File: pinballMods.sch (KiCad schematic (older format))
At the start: 17 parts, among them J1 Conn_01x07_MountingPin, J2 Conn_02x07_Counter_Clockwise_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, J3 Conn_01x07_MountingPin

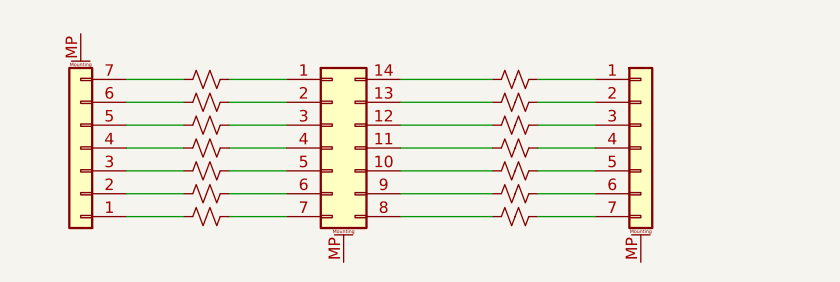
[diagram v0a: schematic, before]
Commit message: Update To Socket and pins
Added DIP16 socket and extra set of pins and pads for 0805 0Ohm resistors.
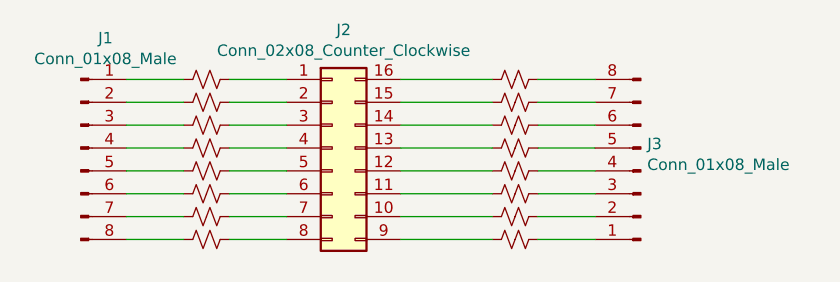
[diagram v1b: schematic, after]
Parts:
- removed J1, J3: Conn_01x07_MountingPin, Connector_PinHeader_2.54mm:PinHeader_1x07_P2.54mm_Vertical, symbol Connector_Generic_MountingPin:Conn_01x07_MountingPin
- removed J2: Conn_02x07_Counter_Clockwise_MountingPin, Package_DIP:DIP-14_W7.62mm_Socket_LongPads, symbol Connector_Generic_MountingPin:Conn_02x07_Counter_Clockwise_MountingPin
- added J1, J3: Conn_01x08_Male, Connector_PinHeader_2.54mm:PinHeader_1x08_P2.54mm_Vertical, symbol Connector:Conn_01x08_Male
- added J2: Conn_02x08_Counter_Clockwise, Package_DIP:DIP-16_W7.62mm_Socket, symbol Connector_Generic:Conn_02x08_Counter_Clockwise
- added R16, R8: R_Small_US, Resistor_SMD:R_0805_2012Metric_Pad1.20x1.40mm_HandSolder, symbol Device:R_Small_US
- R2: value R1 -> R2
- renumbered R9 to R10, R10 to R11, R11 to R12, R12 to R13, R13 to R14, R14 to R15, R8 to R9
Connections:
- net at R1.2: now also J2.1 (Pin_1)
- net at R13.1: now also J2.12 (Pin_12)
- net at R12.1: now also J2.13 (Pin_13)
- net at R11.1: now also J2.14 (Pin_14)
- net at R10.1: now also J2.15 (Pin_15)
- net at R9.1: now also J2.16 (Pin_16)
- net at R2.2: now also J2.2 (Pin_2)
- net at R3.2: now also J2.3 (Pin_3)
- net at R4.2: now also J2.4 (Pin_4)
- net at R5.2: now also J2.5 (Pin_5)
- net at R6.2: now also J2.6 (Pin_6)
- net at R7.2: now also J2.7 (Pin_7)
- net at R15.1: now also J2.10 (Pin_10)
- net at R14.1: now also J2.11 (Pin_11)
- net at R9.2: now also J3.8 (Pin_8)
- net at R10.2: now also J3.7 (Pin_7)
- net at R11.2: now also J3.6 (Pin_6)
- net at R12.2: now also J3.5 (Pin_5)
- net at R13.2: now also J3.4 (Pin_4)
- net at R14.2: now also J3.3 (Pin_3)
- net at R15.2: now also J3.2 (Pin_2)
- net at R1.1: now also J1.1 (Pin_1)
- net at R2.1: now also J1.2 (Pin_2)
- net at R3.1: now also J1.3 (Pin_3)
- net at R4.1: now also J1.4 (Pin_4)
- net at R5.1: now also J1.5 (Pin_5)
- net at R6.1: now also J1.6 (Pin_6)
- net at R7.1: now also J1.7 (Pin_7)
- new net: J1.8 (Pin_8), R8.1
- new net: J2.8 (Pin_8), R8.2
- new net: J2.9 (Pin_9), R16.1
- new net: J3.1 (Pin_1), R16.2
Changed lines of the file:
@@
 $EndDescr
 $Comp
-L Connector_Generic_MountingPin:Conn_02x07_Counter_Clockwise_MountingPin J2
-U 1 1 5FF3D6BF
-P 5350 3650
-F 0 "J2" H 5400 4167 50  0001 C CNN
-F 1 "Conn_02x07_Counter_Clockwise_MountingPin" H 5350 2950 50  0001 C CNN
-F 2 "Package_DIP:DIP-14_W7.62mm_Socket_LongPads" H 5350 3650 50  0001 C CNN
-F 3 "~" H 5350 3650 50  0001 C CNN
-	1    5350 3650
-	1    0    0    -1
-$EndComp
-$Comp
-L Device:R_Small_US R8
+L Device:R_Small_US R9
 U 1 1 5FF4481B
 P 6150 3350
-F 0 "R8" V 6263 3350 50  0001 C CNN
+F 0 "R9" V 6263 3350 50  0001 C CNN
 F 1 "R_Small_US" V 6264 3350 50  0001 C CNN
 F 2 "Resistor_SMD:R_0805_2012Metric_Pad1.20x1.40mm_HandSolder" H 6150 3350 50  0001 C CNN
@@
 $EndComp
 $Comp
-L Device:R_Small_US R9
+L Device:R_Small_US R10
 U 1 1 5FF45935
 P 6150 3450
-F 0 "R9" V 6263 3450 50  0001 C CNN
+F 0 "R10" V 6263 3450 50  0001 C CNN
 F 1 "R_Small_US" V 6264 3450 50  0001 C CNN
 F 2 "Resistor_SMD:R_0805_2012Metric_Pad1.20x1.40mm_HandSolder" H 6150 3450 50  0001 C CNN
@@
 $EndComp
 $Comp
-L Device:R_Small_US R10
+L Device:R_Small_US R11
 U 1 1 5FF461A4
 P 6150 3550
-F 0 "R10" V 6263 3550 50  0001 C CNN
+F 0 "R11" V 6263 3550 50  0001 C CNN
 F 1 "R_Small_US" V 6264 3550 50  0001 C CNN
 F 2 "Resistor_SMD:R_0805_2012Metric_Pad1.20x1.40mm_HandSolder" H 6150 3550 50  0001 C CNN
@@
 $EndComp
 $Comp
-L Device:R_Small_US R11
+L Device:R_Small_US R12
 U 1 1 5FF466FC
 P 6150 3650
-F 0 "R11" V 6263 3650 50  0001 C CNN
+F 0 "R12" V 6263 3650 50  0001 C CNN
 F 1 "R_Small_US" V 6264 3650 50  0001 C CNN
 F 2 "Resistor_SMD:R_0805_2012Metric_Pad1.20x1.40mm_HandSolder" H 6150 3650 50  0001 C CNN
@@
 $EndComp
 $Comp
-L Device:R_Small_US R12
+L Device:R_Small_US R13
 U 1 1 5FF4686E
 P 6150 3750
-F 0 "R12" V 6263 3750 50  0001 C CNN
+F 0 "R13" V 6263 3750 50  0001 C CNN
 F 1 "R_Small_US" V 6264 3750 50  0001 C CNN
 F 2 "Resistor_SMD:R_0805_2012Metric_Pad1.20x1.40mm_HandSolder" H 6150 3750 50  0001 C CNN
@@
 $EndComp
 $Comp
-L Device:R_Small_US R13
+L Device:R_Small_US R14
 U 1 1 5FF46986
 P 6150 3850
-F 0 "R13" V 6263 3850 50  0001 C CNN
+F 0 "R14" V 6263 3850 50  0001 C CNN
 F 1 "R_Small_US" V 6264 3850 50  0001 C CNN
 F 2 "Resistor_SMD:R_0805_2012Metric_Pad1.20x1.40mm_HandSolder" H 6150 3850 50  0001 C CNN
@@
 $EndComp
 $Comp
-L Device:R_Small_US R14
+L Device:R_Small_US R15
 U 1 1 5FF46B0A
 P 6150 3950
-F 0 "R14" V 6263 3950 50  0001 C CNN
+F 0 "R15" V 6263 3950 50  0001 C CNN
 F 1 "R_Small_US" V 6264 3950 50  0001 C CNN
 F 2 "Resistor_SMD:R_0805_2012Metric_Pad1.20x1.40mm_HandSolder" H 6150 3950 50  0001 C CNN
@@
 P 4800 3450
 F 0 "R2" V 4913 3450 50  0001 C CNN
-F 1 "R1" V 4914 3450 50  0001 C CNN
+F 1 "R2" V 4914 3450 50  0001 C CNN
 F 2 "Resistor_SMD:R_0805_2012Metric_Pad1.20x1.40mm_HandSolder" H 4800 3450 50  0001 C CNN
 F 3 "~" H 4800 3450 50  0001 C CNN
@@
 Wire Wire Line
 	5650 3350 6050 3350
-$Comp
-L Connector_Generic_MountingPin:Conn_01x07_MountingPin J1
-U 1 1 5FF55A6E
+Wire Wire Line
+	4450 3350 4700 3350
+Wire Wire Line
+	4700 3450 4450 3450
+Wire Wire Line
+	4450 3550 4700 3550
+Wire Wire Line
+	4700 3650 4450 3650
+Wire Wire Line
+	4450 3750 4700 3750
+Wire Wire Line
+	4700 3850 4450 3850
+Wire Wire Line
+	4450 3950 4700 3950
+Wire Wire Line
+	6250 3350 6500 3350
+Wire Wire Line
+	6500 3450 6250 3450
+Wire Wire Line
+	6250 3550 6500 3550
+Wire Wire Line
+	6500 3650 6250 3650
+Wire Wire Line
+	6250 3750 6500 3750
+Wire Wire Line
+	6500 3850 6250 3850
+Wire Wire Line
+	6250 3950 6500 3950
+$Comp
+L Device:R_Small_US R8
+U 1 1 600A6520
+P 4800 4050
+F 0 "R8" V 5005 4050 50  0001 C CNN
+F 1 "R_Small_US" V 4913 4050 50  0001 C CNN
+F 2 "Resistor_SMD:R_0805_2012Metric_Pad1.20x1.40mm_HandSolder" H 4800 4050 50  0001 C CNN
+F 3 "~" H 4800 4050 50  0001 C CNN
+	1    4800 4050
+	0    -1   -1   0
+$EndComp
+$Comp
+L Device:R_Small_US R16
+U 1 1 600A6C48
+P 6150 4050
+F 0 "R16" V 6263 4050 50  0001 C CNN
+F 1 "R_Small_US" V 6264 4050 50  0001 C CNN
+F 2 "Resistor_SMD:R_0805_2012Metric_Pad1.20x1.40mm_HandSolder" H 6150 4050 50  0001 C CNN
+F 3 "~" H 6150 4050 50  0001 C CNN
+	1    6150 4050
+	0    -1   -1   0
+$EndComp
+$Comp
+L Connector:Conn_01x08_Male J1
+U 1 1 600A8ACB
 P 4250 3650
-F 0 "J1" H 4337 3568 50  0001 L CNN
-F 1 "Conn_01x07_MountingPin" H 4338 3613 50  0001 L CNN
-F 2 "Connector_PinHeader_2.54mm:PinHeader_1x07_P2.54mm_Vertical" H 4250 3650 50  0001 C CNN
+F 0 "J1" H 4358 4131 50  0000 C CNN
+F 1 "Conn_01x08_Male" H 4358 4040 50  0000 C CNN
+F 2 "Connector_PinHeader_2.54mm:PinHeader_1x08_P2.54mm_Vertical" H 4250 3650 50  0001 C CNN
 F 3 "~" H 4250 3650 50  0001 C CNN
 	1    4250 3650
+	1    0    0    -1
+$EndComp
+$Comp
+L Connector:Conn_01x08_Male J3
+U 1 1 600A9E0D
+P 6700 3750
+F 0 "J3" H 6672 3632 50  0000 R CNN
+F 1 "Conn_01x08_Male" H 6672 3723 50  0000 R CNN
+F 2 "Connector_PinHeader_2.54mm:PinHeader_1x08_P2.54mm_Vertical" H 6700 3750 50  0001 C CNN
+F 3 "~" H 6700 3750 50  0001 C CNN
+	1    6700 3750
 	-1   0    0    1
 $EndComp
 $Comp
-L Connector_Generic_MountingPin:Conn_01x07_MountingPin J3
-U 1 1 5FF56D5A
-P 6700 3650
-F 0 "J3" H 6788 3568 50  0001 L CNN
-F 1 "Conn_01x07_MountingPin" H 6788 3523 50  0001 L CNN
-F 2 "Connector_PinHeader_2.54mm:PinHeader_1x07_P2.54mm_Vertical" H 6700 3650 50  0001 C CNN
-F 3 "~" H 6700 3650 50  0001 C CNN
-	1    6700 3650
+L Connector_Generic:Conn_02x08_Counter_Clockwise J2
+U 1 1 600ABC38
+P 5350 3650
+F 0 "J2" H 5400 4167 50  0000 C CNN
+F 1 "Conn_02x08_Counter_Clockwise" H 5400 4076 50  0000 C CNN
+F 2 "Package_DIP:DIP-16_W7.62mm_Socket" H 5350 3650 50  0001 C CNN
+F 3 "~" H 5350 3650 50  0001 C CNN
+	1    5350 3650
 	1    0    0    -1
 $EndComp
 Wire Wire Line
-	4450 3350 4700 3350
-Wire Wire Line
-	4700 3450 4450 3450
-Wire Wire Line
-	4450 3550 4700 3550
-Wire Wire Line
-	4700 3650 4450 3650
-Wire Wire Line
-	4450 3750 4700 3750
-Wire Wire Line
-	4700 3850 4450 3850
-Wire Wire Line
-	4450 3950 4700 3950
-Wire Wire Line
-	6250 3350 6500 3350
-Wire Wire Line
-	6500 3450 6250 3450
-Wire Wire Line
-	6250 3550 6500 3550
-Wire Wire Line
-	6500 3650 6250 3650
-Wire Wire Line
-	6250 3750 6500 3750
-Wire Wire Line
-	6500 3850 6250 3850
-Wire Wire Line
-	6250 3950 6500 3950
+	4450 4050 4700 4050
+Wire Wire Line
+	4900 4050 5150 4050
+Wire Wire Line
+	5650 4050 6050 4050
+Wire Wire Line
+	6250 4050 6500 4050
 $EndSCHEMATC
